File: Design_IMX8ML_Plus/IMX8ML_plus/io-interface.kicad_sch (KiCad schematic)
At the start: 1 part, among them U1 MIMX8ML8CVNKZAB

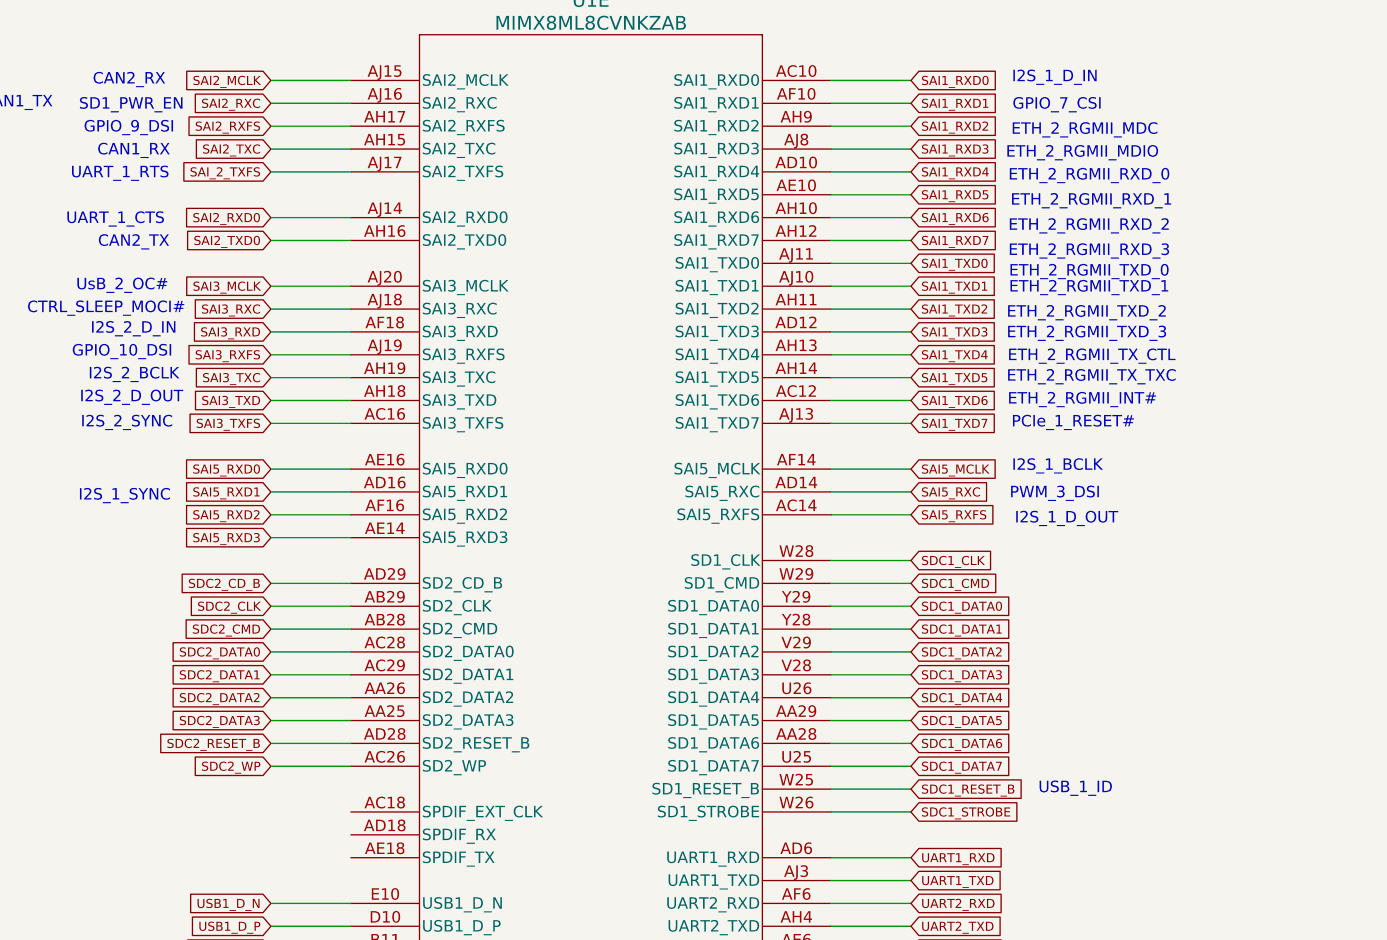
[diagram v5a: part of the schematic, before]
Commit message: [CPU/BB] Improving the conection between the cpu and BB
* Reorganization of the components in the Base board.
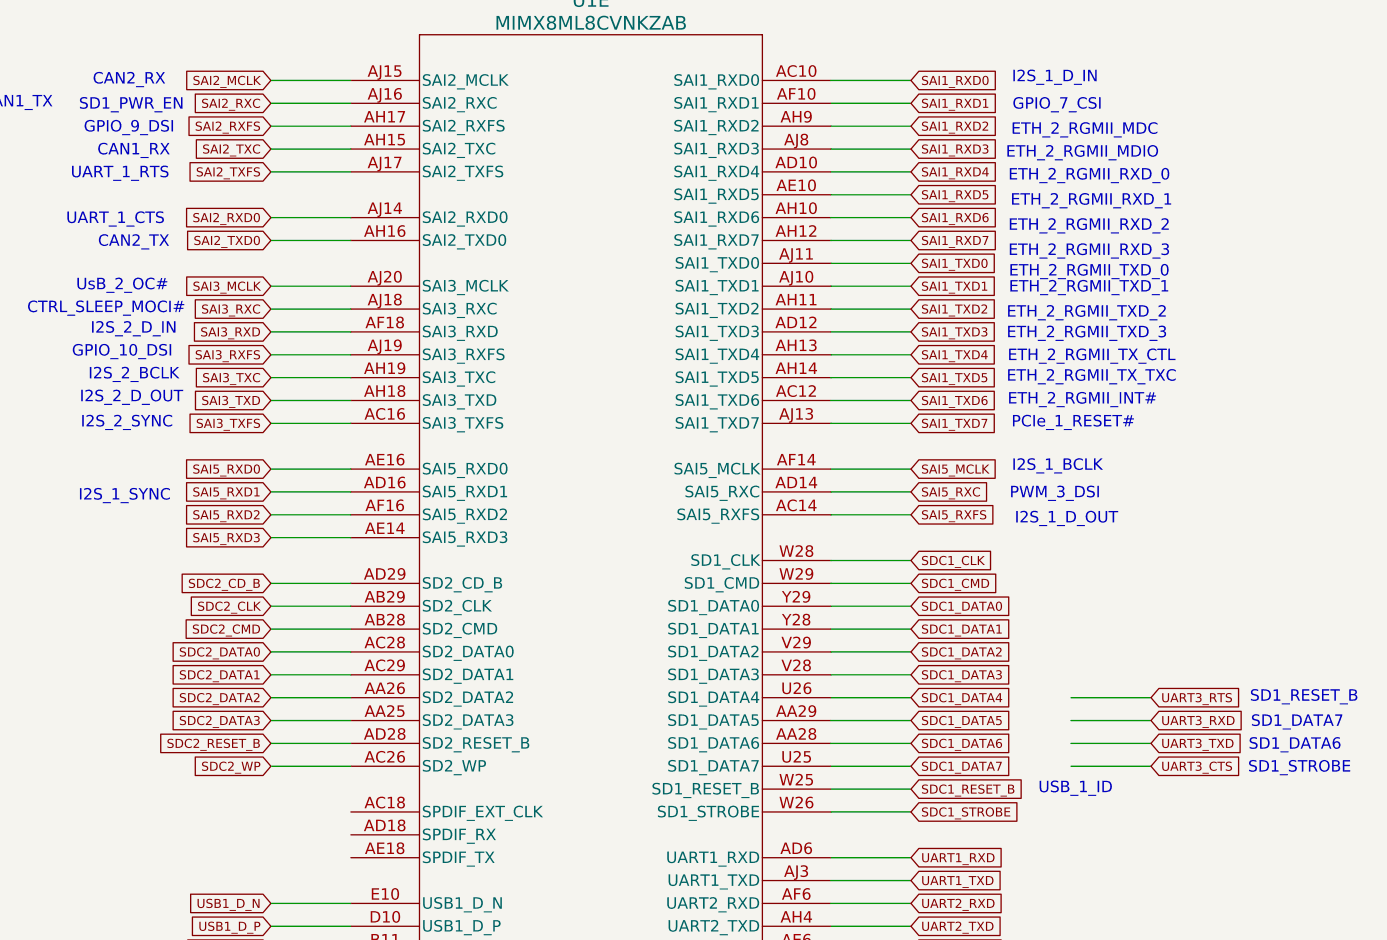
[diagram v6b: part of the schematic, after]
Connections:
- net SAI_2_TXFS renamed SAI2_TXFS
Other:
- note added: "SD1_DATA6"
- note added: "SD1_DATA7"
- note added: "SD1_RESET_B"
- note added: "SD1_STROBE"
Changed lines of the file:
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@@
 	(wire
 		(pts
+			(xy 256.54 104.14) (xy 265.43 104.14)
+		)
+		(stroke
+			(width 0)
+			(type default)
+		)
+	)
+	(wire
+		(pts
 			(xy 176.53 30.48) (xy 167.64 30.48)
 		)
@@
 	(wire
 		(pts
+			(xy 256.54 106.68) (xy 265.43 106.68)
+		)
+		(stroke
+			(width 0)
+			(type default)
+		)
+	)
+	(wire
+		(pts
 			(xy 96.52 92.71) (xy 105.41 92.71)
 		)
@@
 	(wire
 		(pts
+			(xy 256.54 101.6) (xy 265.43 101.6)
+		)
+		(stroke
+			(width 0)
+			(type default)
+		)
+	)
+	(wire
+		(pts
 			(xy 176.53 91.44) (xy 167.64 91.44)
 		)
@@
 	(wire
 		(pts
+			(xy 256.54 99.06) (xy 265.43 99.06)
+		)
+		(stroke
+			(width 0)
+			(type default)
+		)
+	)
+	(wire
+		(pts
 			(xy 229.87 109.22) (xy 238.76 109.22)
 		)
@@
 		)
 	)
+	(text "SD1_DATA6"
+		(exclude_from_sim no)
+		(at 281.432 104.394 0)
+		(effects
+			(font
+				(size 1.27 1.27)
+			)
+		)
+	)
 	(text "CAN2_RX"
 		(exclude_from_sim no)
@@
 		)
 	)
+	(text "SD1_STROBE"
+		(exclude_from_sim no)
+		(at 281.94 106.934 0)
+		(effects
+			(font
+				(size 1.27 1.27)
+			)
+		)
+	)
 	(text "I2S_2_SYNC"
 		(exclude_from_sim no)
@@
 		)
 	)
+	(text "SD1_RESET_B"
+		(exclude_from_sim no)
+		(at 282.448 99.06 0)
+		(effects
+			(font
+				(size 1.27 1.27)
+			)
+		)
+	)
 	(text "ETH_2_RGMII_TX_TXC"
 		(exclude_from_sim no)
@@
 		)
 	)
+	(text "SD1_DATA7"
+		(exclude_from_sim no)
+		(at 281.686 101.854 0)
+		(effects
+			(font
+				(size 1.27 1.27)
+			)
+		)
+	)
 	(text "GPIO_7_CSI"
 		(exclude_from_sim no)
@@
 		)
 	)
+	(global_label "UART3_CTS"
+		(shape input)
+		(at 265.43 106.68 0)
+		(fields_autoplaced yes)
+		(effects
+			(font
+				(size 1 1)
+			)
+			(justify left)
+		)
+		(property "Intersheetrefs" "${INTERSHEET_REFS}"
+			(at 275.8755 106.68 0)
+			(effects
+				(font
+					(size 1.27 1.27)
+				)
+				(justify left)
+				(hide yes)
+			)
+		)
+	)
 	(global_label "SAI1_TXD2"
 		(shape input)
@@
 		)
 	)
+	(global_label "UART3_RXD"
+		(shape input)
+		(at 265.43 101.6 0)
+		(fields_autoplaced yes)
+		(effects
+			(font
+				(size 1 1)
+			)
+			(justify left)
+		)
+		(property "Intersheetrefs" "${INTERSHEET_REFS}"
+			(at 276.0512 101.6 0)
+			(effects
+				(font
+					(size 1.27 1.27)
+				)
+				(justify left)
+				(hide yes)
+			)
+		)
+	)
 	(global_label "SAI1_RXD5"
 		(shape input)
@@
 		)
 	)
-	(global_label "SAI_2_TXFS"
+	(global_label "SAI2_TXFS"
 		(shape input)
 		(at 167.64 40.64 180)
@@
 		)
 		(property "Intersheetrefs" "${INTERSHEET_REFS}"
-			(at 157.004 40.64 0)
+			(at 157.7659 40.64 0)
 			(effects
 				(font
@@
 		)
 	)
+	(global_label "UART3_TXD"
+		(shape input)
+		(at 265.43 104.14 0)
+		(fields_autoplaced yes)
+		(effects
+			(font
+				(size 1 1)
+			)
+			(justify left)
+		)
+		(property "Intersheetrefs" "${INTERSHEET_REFS}"
+			(at 275.8131 104.14 0)
+			(effects
+				(font
+					(size 1.27 1.27)
+				)
+				(justify left)
+				(hide yes)
+			)
+		)
+	)
 	(global_label "HDMI_TXC_N"
 		(shape input)
@@
 			(effects
 				(font
+					(size 1.27 1.27)
+				)
+				(justify left)
+				(hide yes)
+			)
+		)
+	)
+	(global_label "UART3_RTS"
+		(shape input)
+		(at 265.43 99.06 0)
+		(fields_autoplaced yes)
+		(effects
+			(font
+				(size 1 1)
+			)
+			(justify left)
+		)
+		(property "Intersheetrefs" "${INTERSHEET_REFS}"
+			(at 275.8755 99.06 0)
+			(effects
+				(font

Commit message: [BB_IMX8MLP IMX8MLP] Actuallizated to 9.0 kicad version
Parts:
- U1: footprint LFBGA548_SOT2047-1_NXP -> _W_SBC:LFBGA548_SOT2047-1_NXP; MP (none) -> -
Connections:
- net GPIO1_IO02 renamed WDOG_B
- net GPIO1_IO03 renamed PMC_nINT
- net GPIO1_IO04 renamed SD2_VSEL

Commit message: [IMX8ML] Add new layer
A new layers was add in the cpu schematic, now it had 8 layer.
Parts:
- added R41: 8.2K, Resistor_SMD:R_0201_0603Metric, symbol Device:R_Small
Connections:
- net SPDIF_EXT_CLK: now reaches U1.AC18 (SPDIF_EXT_CLK)
- net SPDIF_RX: now reaches U1.AD18 (SPDIF_RX)
- net SPDIF_TX: now reaches U1.AE18 (SPDIF_TX)
- net at U1.AJ28 (HDMI_REXT): no longer names the net of U1.AJ28 (HDMI_REXT)
- net at U1.AJ28 (HDMI_REXT): now also R41.1
- net SDC1_DATA6 renamed UART3_TXD_WiFi
- net SDC1_DATA7 renamed UART3_RXD_WiFi
- net SDC1_RESET_B renamed UART3_RTS_WiFi
- net SDC1_STROBE renamed UART3_CTS_WiFi
- new net GND: R41.2
